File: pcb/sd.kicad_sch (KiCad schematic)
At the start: 1 part

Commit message: everything except crystal
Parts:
- added C?: 10u, symbol Device:C_Polarized_US
- added C?: 100n, symbol Device:C
- added R? (x5): 22, symbol Device:R
- added R? (x3): 47k, symbol Device:R
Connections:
- net +3.3V: now also C?.1, C?.1, R?.1, R?.1, R?.1
- net GND: now also C?.2, C?.2; no longer J?.11 (WP)
- net MCU_SD_US0_CLK: now also R?.1; no longer J?.5 (CLK)
- net MCU_SD_US0_CS: now also R?.2, R?.2; no longer J?.1 (CD/DAT3)
- net MCU_SD_US0_MISO: now also R?.2; no longer J?.7 (DAT0)
- net MCU_SD_US0_MOSI: now also R?.1; no longer J?.2 (CMD)
- net SD_CARD_DETECT: now also R?.2; no longer J?.10 (CD)
- net at J?.8 (DAT1): now also R?.2
- net at J?.9 (DAT2): now also R?.2
- new net: J?.1 (CD/DAT3), R?.1
- new net: J?.10 (CD), R?.1
- new net: J?.2 (CMD), R?.2
- new net: J?.5 (CLK), R?.2
- new net: J?.7 (DAT0), R?.1
- no-connect marks 2 -> 1
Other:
- note removed: "NOT SURE IF WE SHOULD PUT WP TO GND?"

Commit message: add footprints
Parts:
- C801: renamed from C?; footprint (none) -> Capacitor_SMD:C_0603_1608Metric_Pad1.08x0.95mm_HandSolder
- C802: renamed from C?; footprint (none) -> Capacitor_SMD:C_0805_2012Metric_Pad1.18x1.45mm_HandSolder
- R801, R802, R803, R804, R805, R806, R807, R808: renamed from R?; footprint (none) -> Resistor_SMD:R_0805_2012Metric_Pad1.20x1.40mm_HandSolder
- gave numbers to parts that had none: 1
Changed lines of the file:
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@@
   (symbol (lib_id "sd:10067847-001RLF") (at 107.95 82.55 0) (unit 1)
     (in_bom yes) (on_board yes) (fields_autoplaced)
-    (property "Reference" "J?" (id 0) (at 130.81 68.58 0)
+    (property "Reference" "J801" (id 0) (at 130.81 68.58 0)
       (effects (font (size 1.524 1.524)))
     )
@@
   (symbol (lib_id "Device:R") (at 166.37 82.55 90) (unit 1)
     (in_bom yes) (on_board yes)
-    (property "Reference" "R?" (id 0) (at 170.18 81.28 90))
+    (property "Reference" "R805" (id 0) (at 170.18 81.28 90))
     (property "Value" "22" (id 1) (at 166.37 82.55 90))
-    (property "Footprint" "" (id 2) (at 166.37 84.328 90)
+    (property "Footprint" "Resistor_SMD:R_0805_2012Metric_Pad1.20x1.40mm_HandSolder" (id 2) (at 166.37 84.328 90)
       (effects (font (size 1.27 1.27)) hide)
     )
@@
   (symbol (lib_id "Device:C_Polarized_US") (at 196.85 132.08 0) (unit 1)
     (in_bom yes) (on_board yes)
-    (property "Reference" "C?" (id 0) (at 200.66 130.81 0)
+    (property "Reference" "C802" (id 0) (at 200.66 130.81 0)
       (effects (font (size 1.27 1.27)) (justify left))
     )
@@
       (effects (font (size 1.27 1.27)) (justify left))
     )
-    (property "Footprint" "" (id 2) (at 196.85 132.08 0)
+    (property "Footprint" "Capacitor_SMD:C_0805_2012Metric_Pad1.18x1.45mm_HandSolder" (id 2) (at 196.85 132.08 0)
       (effects (font (size 1.27 1.27)) hide)
     )
@@
   (symbol (lib_id "Device:R") (at 166.37 85.09 90) (unit 1)
     (in_bom yes) (on_board yes)
-    (property "Reference" "R?" (id 0) (at 170.18 86.36 90))
+    (property "Reference" "R806" (id 0) (at 170.18 86.36 90))
     (property "Value" "22" (id 1) (at 166.37 85.09 90))
-    (property "Footprint" "" (id 2) (at 166.37 86.868 90)
+    (property "Footprint" "Resistor_SMD:R_0805_2012Metric_Pad1.20x1.40mm_HandSolder" (id 2) (at 166.37 86.868 90)
       (effects (font (size 1.27 1.27)) hide)
     )
@@
   (symbol (lib_id "power:GND") (at 107.95 115.57 0) (unit 1)
     (in_bom yes) (on_board yes) (fields_autoplaced)
-    (property "Reference" "#PWR?" (id 0) (at 107.95 121.92 0)
+    (property "Reference" "#PWR0801" (id 0) (at 107.95 121.92 0)
       (effects (font (size 1.27 1.27)) hide)
     )
@@
   (symbol (lib_id "Device:R") (at 153.67 110.49 180) (unit 1)
     (in_bom yes) (on_board yes)
-    (property "Reference" "R?" (id 0) (at 151.13 110.49 90))
+    (property "Reference" "R803" (id 0) (at 151.13 110.49 90))
     (property "Value" "47k" (id 1) (at 153.67 110.49 90))
-    (property "Footprint" "" (id 2) (at 155.448 110.49 90)
+    (property "Footprint" "Resistor_SMD:R_0805_2012Metric_Pad1.20x1.40mm_HandSolder" (id 2) (at 155.448 110.49 90)
       (effects (font (size 1.27 1.27)) hide)
     )
@@
   (symbol (lib_id "Device:C") (at 184.15 132.08 0) (unit 1)
     (in_bom yes) (on_board yes) (fields_autoplaced)
-    (property "Reference" "C?" (id 0) (at 187.325 130.8099 0)
+    (property "Reference" "C801" (id 0) (at 187.325 130.8099 0)
       (effects (font (size 1.27 1.27)) (justify left))
     )
@@
       (effects (font (size 1.27 1.27)) (justify left))
     )
-    (property "Footprint" "" (id 2) (at 185.1152 135.89 0)
+    (property "Footprint" "Capacitor_SMD:C_0603_1608Metric_Pad1.08x0.95mm_HandSolder" (id 2) (at 185.1152 135.89 0)
       (effects (font (size 1.27 1.27)) hide)
     )
@@
   (symbol (lib_id "power:+3.3V") (at 196.85 128.27 0) (unit 1)
     (in_bom yes) (on_board yes) (fields_autoplaced)
-    (property "Reference" "#PWR?" (id 0) (at 196.85 132.08 0)
+    (property "Reference" "#PWR0802" (id 0) (at 196.85 132.08 0)
       (effects (font (size 1.27 1.27)) hide)
     )
@@
   (symbol (lib_id "Device:R") (at 160.02 110.49 180) (unit 1)
     (in_bom yes) (on_board yes)
-    (property "Reference" "R?" (id 0) (at 157.48 111.76 90)
+    (property "Reference" "R804" (id 0) (at 157.48 111.76 90)
       (effects (font (size 1.27 1.27)) (justify right))
     )
@@
       (effects (font (size 1.27 1.27)) (justify right))
     )
-    (property "Footprint" "" (id 2) (at 161.798 110.49 90)
+    (property "Footprint" "Resistor_SMD:R_0805_2012Metric_Pad1.20x1.40mm_HandSolder" (id 2) (at 161.798 110.49 90)
       (effects (font (size 1.27 1.27)) hide)
     )
@@
   (symbol (lib_id "power:GND") (at 196.85 135.89 0) (unit 1)
     (in_bom yes) (on_board yes) (fields_autoplaced)
-    (property "Reference" "#PWR?" (id 0) (at 196.85 142.24 0)
+    (property "Reference" "#PWR0803" (id 0) (at 196.85 142.24 0)
       (effects (font (size 1.27 1.27)) hide)
     )
@@
   (symbol (lib_id "Device:R") (at 100.33 82.55 90) (unit 1)
     (in_bom yes) (on_board yes)
-    (property "Reference" "R?" (id 0) (at 104.14 81.28 90))
+    (property "Reference" "R801" (id 0) (at 104.14 81.28 90))
     (property "Value" "22" (id 1) (at 100.33 82.55 90))
-    (property "Footprint" "" (id 2) (at 100.33 84.328 90)
+    (property "Footprint" "Resistor_SMD:R_0805_2012Metric_Pad1.20x1.40mm_HandSolder" (id 2) (at 100.33 84.328 90)
       (effects (font (size 1.27 1.27)) hide)
     )
@@
   (symbol (lib_id "Device:R") (at 173.99 110.49 180) (unit 1)
     (in_bom yes) (on_board yes)
-    (property "Reference" "R?" (id 0) (at 171.45 111.76 90)
+    (property "Reference" "R808" (id 0) (at 171.45 111.76 90)
       (effects (font (size 1.27 1.27)) (justify right))
     )
@@
       (effects (font (size 1.27 1.27)) (justify right))
     )
-    (property "Footprint" "" (id 2) (at 175.768 110.49 90)
+    (property "Footprint" "Resistor_SMD:R_0805_2012Metric_Pad1.20x1.40mm_HandSolder" (id 2) (at 175.768 110.49 90)
       (effects (font (size 1.27 1.27)) hide)
     )
@@
   (symbol (lib_id "Device:R") (at 100.33 85.09 90) (unit 1)
     (in_bom yes) (on_board yes)
-    (property "Reference" "R?" (id 0) (at 104.14 86.36 90))
+    (property "Reference" "R802" (id 0) (at 104.14 86.36 90))
     (property "Value" "22" (id 1) (at 100.33 85.09 90))
-    (property "Footprint" "" (id 2) (at 100.33 86.868 90)
+    (property "Footprint" "Resistor_SMD:R_0805_2012Metric_Pad1.20x1.40mm_HandSolder" (id 2) (at 100.33 86.868 90)
       (effects (font (size 1.27 1.27)) hide)
     )
@@
   (symbol (lib_id "Device:R") (at 166.37 90.17 90) (unit 1)
     (in_bom yes) (on_board yes)
-    (property "Reference" "R?" (id 0) (at 170.18 91.44 90))
+    (property "Reference" "R807" (id 0) (at 170.18 91.44 90))
     (property "Value" "22" (id 1) (at 166.37 90.17 90))
-    (property "Footprint" "" (id 2) (at 166.37 91.948 90)
-      (effects (font (size 1.27 1.27)) hide)
-    )
+    (property "Footprint" "Resistor_SMD:R_0805_2012Metric_Pad1.20x1.40mm_HandSolder" (id 2) (at 166.37 91.948 90)
+      (effects (font (size 1.27 1.27)) hide)
+    )

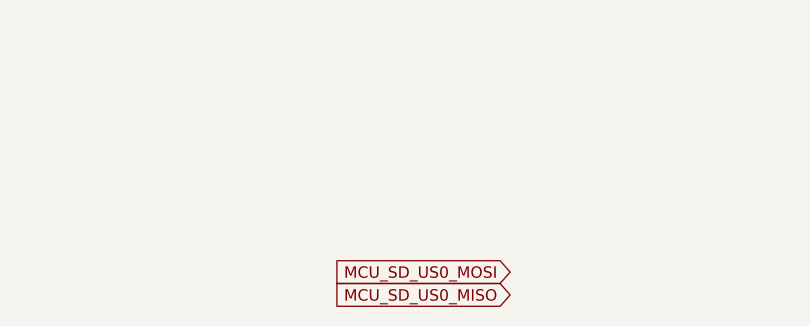
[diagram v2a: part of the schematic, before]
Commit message: add footprints + fix unnconnected
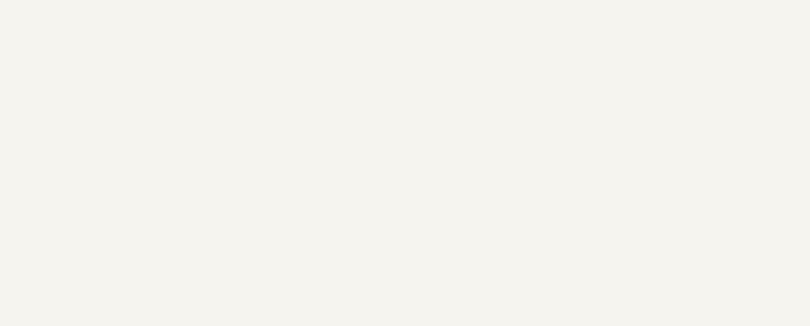
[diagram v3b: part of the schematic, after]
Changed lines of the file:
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@@
-    )
-  )
-  (global_label "MCU_SD_US0_MOSI" (shape input) (at 177.8 190.5 180) (fields_autoplaced)
-    (effects (font (size 1.27 1.27)) (justify right))
-    (property "Intersheet References" "${INTERSHEET_REFS}" (id 0) (at 157.6069 190.4206 0)
-      (effects (font (size 1.27 1.27)) (justify right) hide)
     )
   )
@@
     )
   )
-  (global_label "MCU_SD_US0_MISO" (shape input) (at 177.8 193.04 180) (fields_autoplaced)
-    (effects (font (size 1.27 1.27)) (justify right))
-    (property "Intersheet References" "${INTERSHEET_REFS}" (id 0) (at 157.6069 192.9606 0)
-      (effects (font (size 1.27 1.27)) (justify right) hide)
-    )
-  )

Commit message: assign the last footprints
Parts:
- J801: footprint 10067847-001RLF_AMP -> sd:10067847-001RLF
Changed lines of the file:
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@@
       (effects (font (size 1.524 1.524)))
     )
-    (property "Footprint" "10067847-001RLF_AMP" (id 2) (at 130.81 73.914 0)
+    (property "Footprint" "sd:10067847-001RLF" (id 2) (at 130.81 73.914 0)
       (effects (font (size 1.524 1.524)) hide)
     )

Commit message: fix capacitor values and footprints
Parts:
- C801: footprint Capacitor_SMD:C_0603_1608Metric_Pad1.08x0.95mm_HandSolder -> Capacitor_SMD:C_0805_2012Metric_Pad1.18x1.45mm_HandSolder
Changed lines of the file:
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@@
       (effects (font (size 1.27 1.27)) (justify left))
     )
-    (property "Footprint" "Capacitor_SMD:C_0603_1608Metric_Pad1.08x0.95mm_HandSolder" (id 2) (at 185.1152 135.89 0)
+    (property "Footprint" "Capacitor_SMD:C_0805_2012Metric_Pad1.18x1.45mm_HandSolder" (id 2) (at 185.1152 135.89 0)
       (effects (font (size 1.27 1.27)) hide)
     )
